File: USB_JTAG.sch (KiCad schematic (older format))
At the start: 11 parts, among them J3 Conn_01x06, J5 AVR-JTAG-10, J6 Conn_01x06, SW1 SW_DIP_x03, U2 LTC6930IMS8 7.3728MHz, X1 CB3LV-3I-50M0000

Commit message: added FT JTAG
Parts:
- removed C17: 100nF, Capacitor_SMD:C_0603_1608Metric_Pad1.05x0.95mm_HandSolder, symbol Device:C
- removed R1: 22R5, Resistor_SMD:R_0603_1608Metric_Pad1.05x0.95mm_HandSolder, symbol Device:R_Small
- removed R2, R3, R4: 1K, Resistor_SMD:R_0603_1608Metric_Pad1.05x0.95mm_HandSolder, symbol Device:R_Small
- removed SW1: SW_DIP_x03, Button_Switch_SMD:SW_DIP_SPSTx03_Slide_6.7x9.18mm_W8.61mm_P2.54mm_LowProfile, symbol Switch:SW_DIP_x03
- removed U2: LTC6930IMS8 7.3728MHz, Package_SO:MSOP-8_3x3mm_P0.65mm, symbol Oscillator:LTC6930IMS8
- removed X1: CB3LV-3I-50M0000, Oscillator:Oscillator_SMD_SeikoEpson_SG8002CA-4Pin_7.0x5.0mm_HandSoldering, symbol Oscillator:CB3LV-3I-50M0000
- added C28, C30, C38, C40, C41, C42, C43, C44, C45, C46, C47, C48: 100nF, Capacitor_SMD:C_0603_1608Metric_Pad1.05x0.95mm_HandSolder, symbol Device:C
- added C29: 2.2uF, Capacitor_SMD:C_0603_1608Metric_Pad1.05x0.95mm_HandSolder, symbol Device:C
- added C31, C32: 18pF, Capacitor_SMD:C_0603_1608Metric_Pad1.05x0.95mm_HandSolder, symbol Device:C_Small
- added C37, C39: 4.7uF, Capacitor_SMD:C_0603_1608Metric_Pad1.05x0.95mm_HandSolder, symbol Device:C
- added J7: USB_B_Micro, Connector_USB:USB_Micro-B_Molex-105017-0001, symbol Connector:USB_B_Micro
- added J9: Conn_02x04_Counter_Clockwise, Connector_PinHeader_2.54mm:PinHeader_2x04_P2.54mm_Vertical, symbol Connector_Generic:Conn_02x04_Counter_Clockwise
- added L1, L2: 600ohm, Inductor_SMD:L_0603_1608Metric_Pad1.05x0.95mm_HandSolder, symbol Device:L
- added R16, R17, R18, R20, R21, R22, R23: 10K, Resistor_SMD:R_0603_1608Metric_Pad1.05x0.95mm_HandSolder, symbol Device:R
- added R19: 2K2, Resistor_SMD:R_0603_1608Metric_Pad1.05x0.95mm_HandSolder, symbol Device:R
- added R2: 12K, Resistor_SMD:R_0603_1608Metric_Pad1.05x0.95mm_HandSolder, symbol Device:R
- added R24, R25, R26, R27: 22R, Resistor_SMD:R_0603_1608Metric_Pad1.05x0.95mm_HandSolder, symbol Device:R
- added R3: 1K, Resistor_SMD:R_0603_1608Metric_Pad1.05x0.95mm_HandSolder, symbol Device:R
- added R4: 1M, Resistor_SMD:R_0603_1608Metric_Pad1.05x0.95mm_HandSolder, symbol Device:R
- added U6: TPD2EUSB30, Package_TO_SOT_SMD:Texas_DRT-3, symbol Power_Protection:TPD2EUSB30
- added U7: FT2232H, Package_QFP:LQFP-64_10x10mm_P0.5mm, symbol Interface_USB:FT2232H
- added U8: MIC5356-SGYMME, Package_SO:MSOP-8-1EP_3x3mm_P0.65mm_EP2.5x3mm_Mask1.73x2.36mm_ThermalVias, symbol Regulator_Linear:MIC5356-SGYMME
- added U9: 93LCxxBxxOT, Package_TO_SOT_SMD:SOT-23-6, symbol Memory_EEPROM:93LCxxBxxOT
- added Y1: CTS-445 12Mhz, Crystal:Crystal_SMD_5032-2Pin_5.0x3.2mm_HandSoldering, symbol Device:Crystal
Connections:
- net labels added: +1V8, JTAG_TCK, JTAG_TDI, JTAG_TDO, JTAG_TMS
- net labels removed: IO1_CLK0, IO1_CLK1
- wire segments 44 -> 160
- no-connect marks 0 -> 15
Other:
- moved on the sheet: J5

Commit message: replaced single resistors with arrays
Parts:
- removed J3, J6: Conn_01x06, Connector_PinHeader_2.54mm:PinHeader_1x06_P2.54mm_Horizontal, symbol Connector_Generic:Conn_01x06
- removed J9: Conn_02x04_Counter_Clockwise, Connector_PinHeader_2.54mm:PinHeader_2x04_P2.54mm_Vertical, symbol Connector_Generic:Conn_02x04_Counter_Clockwise
- removed R16, R17, R18, R20, R21, R22, R23: 10K, Resistor_SMD:R_0603_1608Metric_Pad1.05x0.95mm_HandSolder, symbol Device:R
- removed R24, R25, R26, R27: 22R, Resistor_SMD:R_0603_1608Metric_Pad1.05x0.95mm_HandSolder, symbol Device:R
- added RN5, RN7: 10K, Resistor_SMD:R_Array_Concave_4x0603, symbol Device:R_Pack04
- added RN6: 22R, Resistor_SMD:R_Array_Concave_4x0603, symbol Device:R_Pack04
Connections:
- no-connect marks 15 -> 16

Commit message: fixed up GPIO, started layout
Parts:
- U7: renamed from U8; symbol Regulator_Linear:MIC5356-SGYMME -> rc2014_max_v-rescue:MIC5356-SGYMME-Regulator_Linear
- renumbered C37 to C19, C38 to C20, C39 to C21, C40 to C22, C28 to C23, C29 to C24, C30 to C25, C41 to C26, C31 to C27, C32 to C28, C42 to C29, C43 to C30, C44 to C31, C45 to C32, C46 to C33, C47 to C34, C48 to C35, J7 to J6, R2 to R3, R3 to R4, R4 to R5, R19 to R6, RN5 to RN1, RN6 to RN2, RN7 to RN3, U9 to U10, U6 to U8, U7 to U9
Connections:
- no-connect marks 16 -> 18

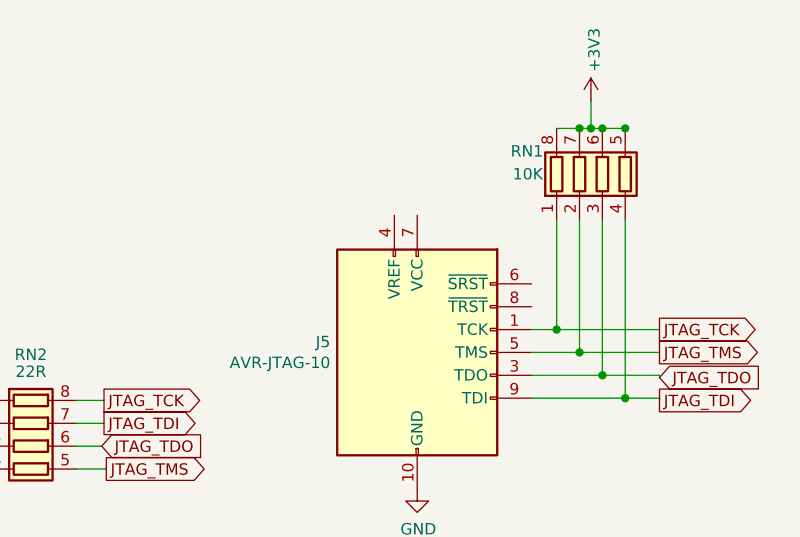
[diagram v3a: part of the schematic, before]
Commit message: Added logo, cpio vcc selection
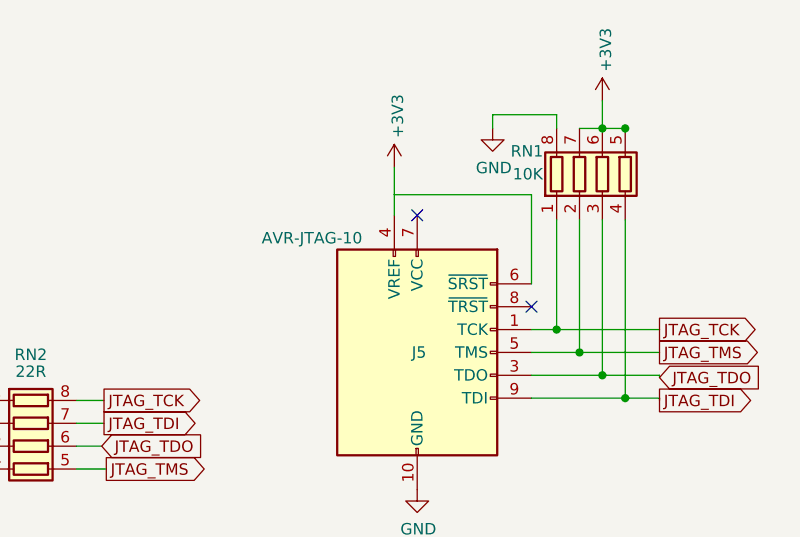
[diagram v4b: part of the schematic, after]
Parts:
- J5: footprint Connector_IDC:IDC-Header_2x05_P2.54mm_Vertical -> Connector_IDC:IDC-Header_2x05_P2.54mm_Horizontal
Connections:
- wire segments 160 -> 165
- no-connect marks 18 -> 20
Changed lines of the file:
@@
 U 1 1 5D0FEAD2
 P 9420 1920
-F 0 "J5" H 9040 1966 50  0000 R CNN
-F 1 "AVR-JTAG-10" H 9040 1875 50  0000 R CNN
-F 2 "Connector_IDC:IDC-Header_2x05_P2.54mm_Vertical" V 9270 2070 50  0001 C CNN
+F 0 "J5" H 9460 1920 50  0000 R CNN
+F 1 "AVR-JTAG-10" H 9180 2420 50  0000 R CNN
+F 2 "Connector_IDC:IDC-Header_2x05_P2.54mm_Horizontal" V 9270 2070 50  0001 C CNN
 F 3 " ~" H 8145 1370 50  0001 C CNN
 	1    9420 1920
@@
 L power:+3V3 #PWR?
 U 1 1 5D1CAEB7
-P 10180 820
+P 10230 820
 AR Path="/5D1CAEB7" Ref="#PWR?"  Part="1"
 AR Path="/5D0F9837/5D1CAEB7" Ref="#PWR027"  Part="1"
-F 0 "#PWR027" H 10180 670 50  0001 C CNN
-F 1 "+3V3" V 10195 948 50  0000 L CNN
-F 2 "" H 10180 820 50  0001 C CNN
-F 3 "" H 10180 820 50  0001 C CNN
-	1    10180 820
+F 0 "#PWR027" H 10230 670 50  0001 C CNN
+F 1 "+3V3" V 10245 948 50  0000 L CNN
+F 2 "" H 10230 820 50  0001 C CNN
+F 3 "" H 10230 820 50  0001 C CNN
+	1    10230 820
 	1    0    0    -1
 $EndComp
@@
 Wire Wire Line
 	6550 1830 6600 1830
-$Comp
-L Device:R_Pack04 RN1
-U 1 1 5CF8ACD2
-P 10230 1140
-AR Path="/5D0F9837/5CF8ACD2" Ref="RN1"  Part="1"
-AR Path="/5CF8ACD2" Ref="RN?"  Part="1"
-AR Path="/5CFABACD/5CF8ACD2" Ref="RN?"  Part="1"
-F 0 "RN1" H 9900 1240 50  0000 C CNN
-F 1 "10K" H 9904 1140 50  0000 C CNN
-F 2 "Resistor_SMD:R_Array_Concave_4x0603" V 10505 1140 50  0001 C CNN
-F 3 "~" H 10230 1140 50  0001 C CNN
-	1    10230 1140
-	1    0    0    -1
-$EndComp
-Wire Wire Line
-	10030 940  10130 940
 Wire Wire Line
 	10330 940  10330 950
-Connection ~ 10330 940
-Connection ~ 10130 940
-Wire Wire Line
-	10130 940  10180 940
-Connection ~ 10230 940
-Wire Wire Line
-	10230 940  10330 940
-Wire Wire Line
-	10180 820  10180 940
-Connection ~ 10180 940
-Wire Wire Line
-	10180 940  10230 940
+Wire Wire Line
+	10230 820  10230 940
 $Comp
 L Device:R_Pack04 RN2
@@
 NoConn ~ 7400 5530
 NoConn ~ 7400 5430
+Wire Wire Line
+	10230 940  10330 940
+Connection ~ 10230 940
+Connection ~ 10330 940
+$Comp
+L Device:R_Pack04 RN1
+U 1 1 5CF8ACD2
+P 10230 1140
+AR Path="/5D0F9837/5CF8ACD2" Ref="RN1"  Part="1"
+AR Path="/5CF8ACD2" Ref="RN?"  Part="1"
+AR Path="/5CFABACD/5CF8ACD2" Ref="RN?"  Part="1"
+F 0 "RN1" H 9900 1240 50  0000 C CNN
+F 1 "10K" H 9904 1140 50  0000 C CNN
+F 2 "Resistor_SMD:R_Array_Concave_4x0603" V 10505 1140 50  0001 C CNN
+F 3 "~" H 10230 1140 50  0001 C CNN
+	1    10230 1140
+	1    0    0    -1
+$EndComp
+Wire Wire Line
+	10130 940  10230 940
+Wire Wire Line
+	10030 940  10030 880
+Wire Wire Line
+	10030 880  9750 880
+Wire Wire Line
+	9750 880  9750 940
+$Comp
+L power:GND #PWR?
+U 1 1 5D1A4182
+P 9750 940
+AR Path="/5D1A4182" Ref="#PWR?"  Part="1"
+AR Path="/5CB63856/5D1A4182" Ref="#PWR?"  Part="1"
+AR Path="/5CB5AB00/5CB63856/5D1A4182" Ref="#PWR?"  Part="1"
+AR Path="/5CFABACD/5D1A4182" Ref="#PWR?"  Part="1"
+AR Path="/5D0F9837/5D1A4182" Ref="#PWR0101"  Part="1"
+F 0 "#PWR0101" H 9750 690 50  0001 C CNN
+F 1 "GND" H 9755 767 50  0000 C CNN
+F 2 "" H 9750 940 50  0001 C CNN
+F 3 "" H 9750 940 50  0001 C CNN
+	1    9750 940
+	1    0    0    -1
+$EndComp
+NoConn ~ 9920 1720
+NoConn ~ 9420 1320
+Wire Wire Line
+	9920 1620 9920 1230
+Wire Wire Line
+	9920 1230 9320 1230
+Wire Wire Line
+	9320 1230 9320 1320
+$Comp
+L power:+3V3 #PWR?
+U 1 1 5D1D069F
+P 9320 1110
+AR Path="/5D1D069F" Ref="#PWR?"  Part="1"
+AR Path="/5D0F9837/5D1D069F" Ref="#PWR0102"  Part="1"
+F 0 "#PWR0102" H 9320 960 50  0001 C CNN
+F 1 "+3V3" V 9335 1238 50  0000 L CNN
+F 2 "" H 9320 1110 50  0001 C CNN
+F 3 "" H 9320 1110 50  0001 C CNN
+	1    9320 1110
+	1    0    0    -1
+$EndComp
+Wire Wire Line
+	9320 1110 9320 1230
 $EndSCHEMATC

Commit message: larger maxv, additional clocks, reorganized sheets
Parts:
- removed C27, C28: 18pF, Capacitor_SMD:C_0603_1608Metric_Pad1.05x0.95mm_HandSolder, symbol Device:C_Small
- removed Y1: CTS-445 12Mhz, Crystal:Crystal_SMD_5032-2Pin_5.0x3.2mm_HandSoldering, symbol Device:Crystal
- added U4: 5M1270ZT144C5N, QFP50P2200X2200X155-144N, symbol CPLD_Altera:5M1270ZT144C5N
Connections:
- net labels added: CLK_12Mhz
- wire segments 165 -> 156
- no-connect marks 20 -> 35
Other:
- moved on the sheet: J5, RN1

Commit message: component placement
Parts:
- added D13: PWR, LED_SMD:LED_0603_1608Metric_Pad1.05x0.95mm_HandSolder, symbol Device:LED
- added R16: 220R, Resistor_SMD:R_0603_1608Metric_Pad1.05x0.95mm_HandSolder, symbol Device:R
- U4: symbol CPLD_Altera:5M1270ZT144C5N -> rc2014_max_v-rescue:5M1270ZT144C5N-CPLD_Altera
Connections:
- net +3V3: now also R16.1
- net at U9.60 (~PWREN): now also D13.1 (K)
- new net: D13.2 (A), R16.2
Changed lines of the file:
@@
 	9290 2770 9290 2890
 $Comp
-L CPLD_Altera:5M1270ZT144C5N U4
+L rc2014_max_v-rescue:5M1270ZT144C5N-CPLD_Altera U4
 U 6 1 5D0AC4AB
 P 9390 4550
+AR Path="/5D0AC4AB" Ref="U4"  Part="6"
+AR Path="/5D0F9837/5D0AC4AB" Ref="U4"  Part="6"
 F 0 "U4" H 9708 4413 50  0000 L CNN
 F 1 "5M1270ZT144C5N" H 9708 4322 50  0000 L CNN
@@
 	4840 5230 5000 5230
 NoConn ~ 5000 5630
+Wire Wire Line
+	7400 5730 7970 5730
+Wire Wire Line
+	7970 5730 7970 5200
+$Comp
+L Device:LED D13
+U 1 1 5CFB1E3B
+P 7970 5050
+F 0 "D13" V 8009 4932 50  0000 R CNN
+F 1 "PWR" V 7918 4932 50  0000 R CNN
+F 2 "LED_SMD:LED_0603_1608Metric_Pad1.05x0.95mm_HandSolder" H 7970 5050 50  0001 C CNN
+F 3 "~" H 7970 5050 50  0001 C CNN
+	1    7970 5050
+	0    -1   -1   0
+$EndComp
+$Comp
+L Device:R R16
+U 1 1 5CFB52C6
+P 7970 4480
+F 0 "R16" H 8040 4540 50  0000 L CNN
+F 1 "220R" H 8040 4470 50  0000 L CNN
+F 2 "Resistor_SMD:R_0603_1608Metric_Pad1.05x0.95mm_HandSolder" V 7900 4480 50  0001 C CNN
+F 3 "~" H 7970 4480 50  0001 C CNN
+	1    7970 4480
+	1    0    0    -1
+$EndComp
+$Comp
+L power:+3V3 #PWR?
+U 1 1 5CFB52CD
+P 7970 4240
+AR Path="/5CFB52CD" Ref="#PWR?"  Part="1"
+AR Path="/5D0F9837/5CFB52CD" Ref="#PWR0107"  Part="1"
+F 0 "#PWR0107" H 7970 4090 50  0001 C CNN
+F 1 "+3V3" V 7985 4368 50  0000 L CNN
+F 2 "" H 7970 4240 50  0001 C CNN
+F 3 "" H 7970 4240 50  0001 C CNN
+	1    7970 4240
+	1    0    0    -1
+$EndComp
+Wire Wire Line
+	7970 4240 7970 4330
+Wire Wire Line
+	7970 4630 7970 4900
 $EndSCHEMATC

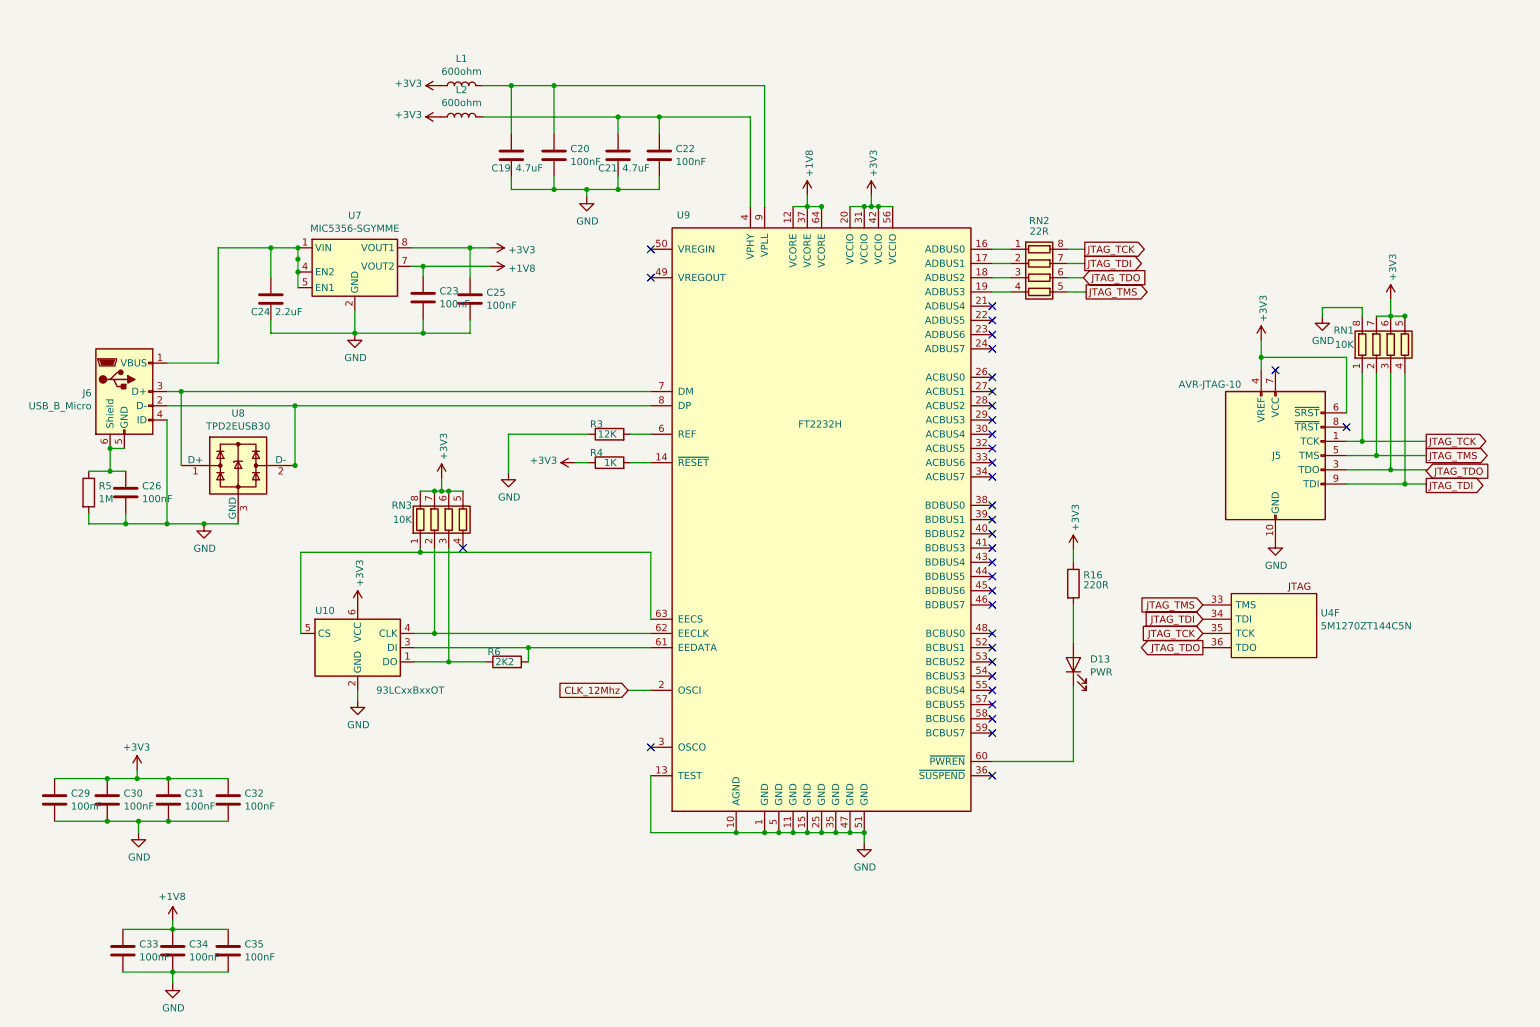
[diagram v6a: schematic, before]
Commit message: fixed errors, connected all pins, switched to 4 layers
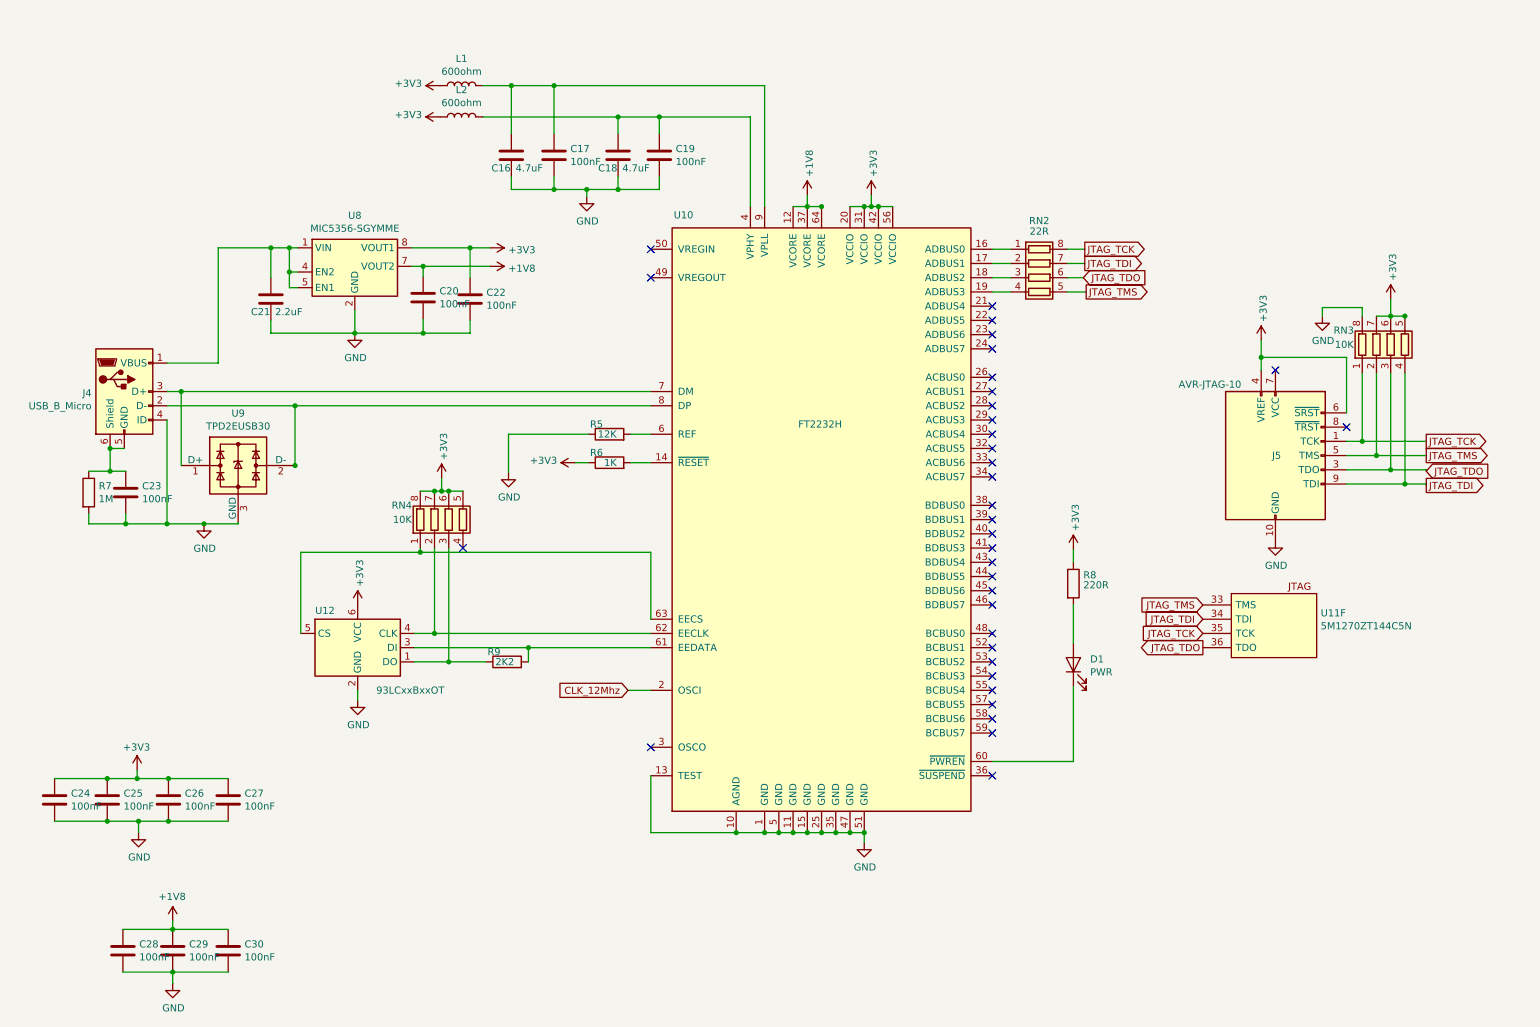
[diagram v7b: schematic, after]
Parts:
- U11: renamed from U4; footprint QFP50P2200X2200X155-144N -> Package_QFP:TQFP-144_20x20mm_P0.5mm
- renumbered C19 to C16, C20 to C17, C21 to C18, C22 to C19, C23 to C20, C24 to C21, C25 to C22, C26 to C23, C29 to C24, C30 to C25, C31 to C26, C32 to C27, C33 to C28, C34 to C29, C35 to C30, D13 to D1, J6 to J4, R3 to R5, R4 to R6, R5 to R7, R16 to R8, R6 to R9, RN1 to RN3, RN3 to RN4, U9 to U10, U10 to U12, U7 to U8, U8 to U9
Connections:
- net at C21.1, J4.1 (VBUS), U8.1 (VIN)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: no longer U8.3 (NC)

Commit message: consolidated power supply
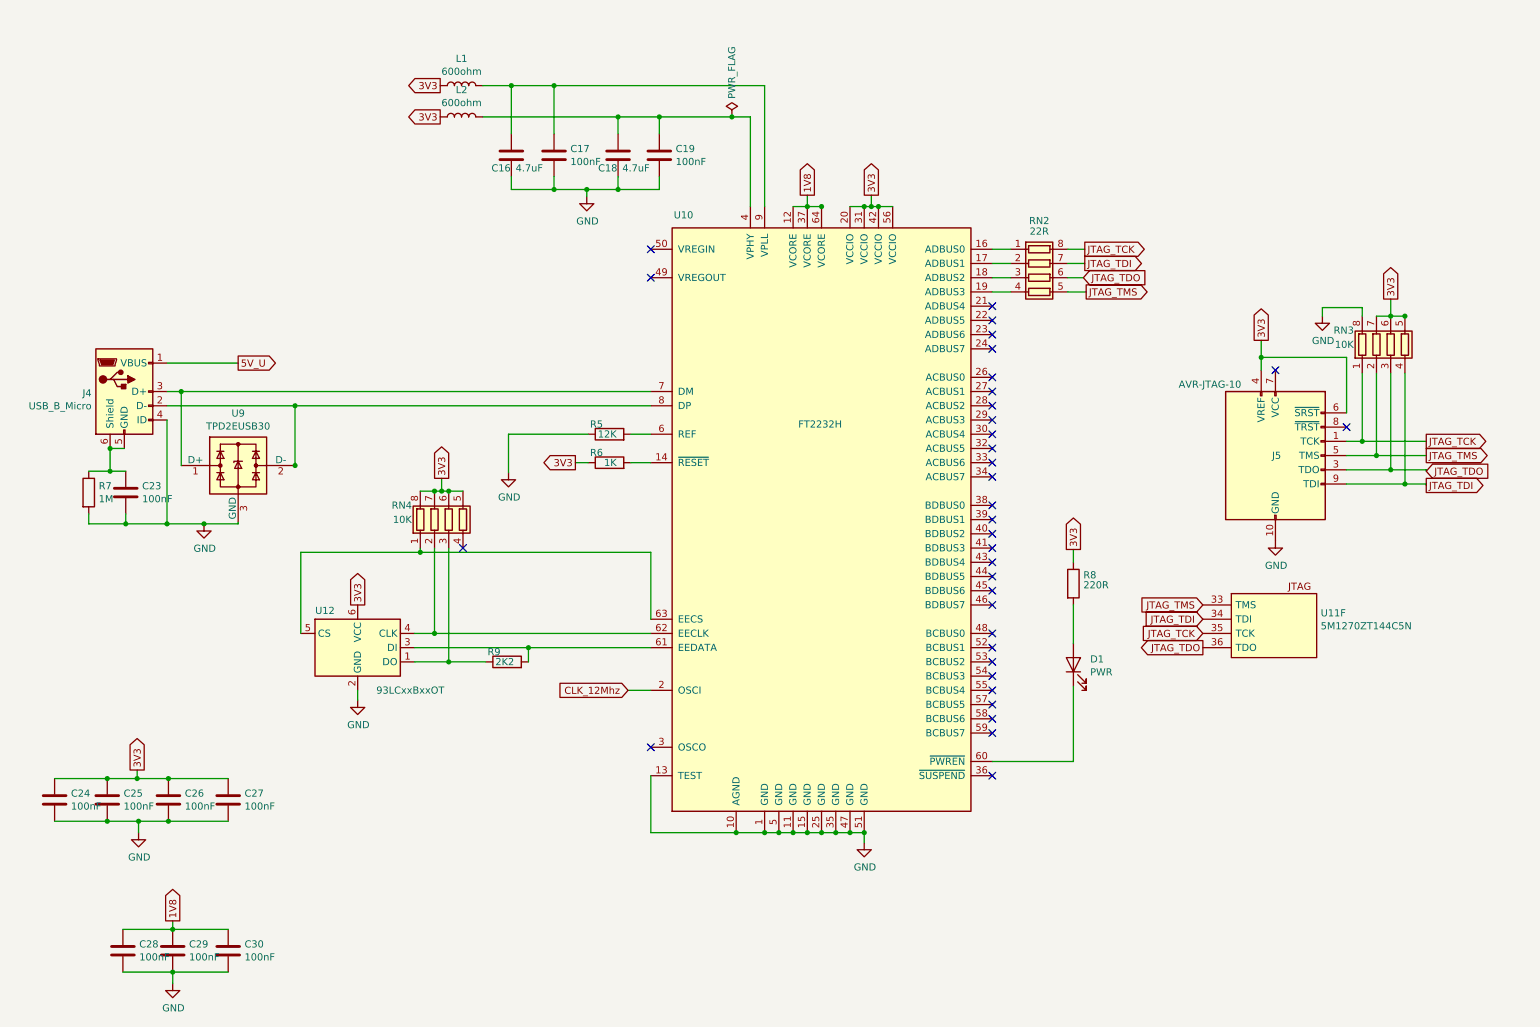
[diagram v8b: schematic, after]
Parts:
- removed C20, C22: 100nF, Capacitor_SMD:C_0603_1608Metric_Pad1.05x0.95mm_HandSolder, symbol Device:C
- removed C21: 2.2uF, Capacitor_SMD:C_0603_1608Metric_Pad1.05x0.95mm_HandSolder, symbol Device:C
- removed U8: MIC5356-SGYMME, Package_SO:MSOP-8-1EP_3x3mm_P0.65mm_EP2.5x3mm_Mask1.73x2.36mm_ThermalVias, symbol rc2014_max_v-rescue:MIC5356-SGYMME-Regulator_Linear
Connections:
- net 5V_U: now reaches J4.1 (VBUS)
- net +1V8 renamed 1V8
- net +3V3 renamed 3V3
